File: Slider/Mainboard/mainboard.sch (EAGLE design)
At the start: 61 parts, among them IC1 7805TV, IC2 33CV, IC3 LM358, Q1 16MHz, SW1 MS MOT1, SW2 MS MOT2, T1 BC337, T2 BC337, U1 ATMEGA328P_PDIP, U2 MAX232PTH

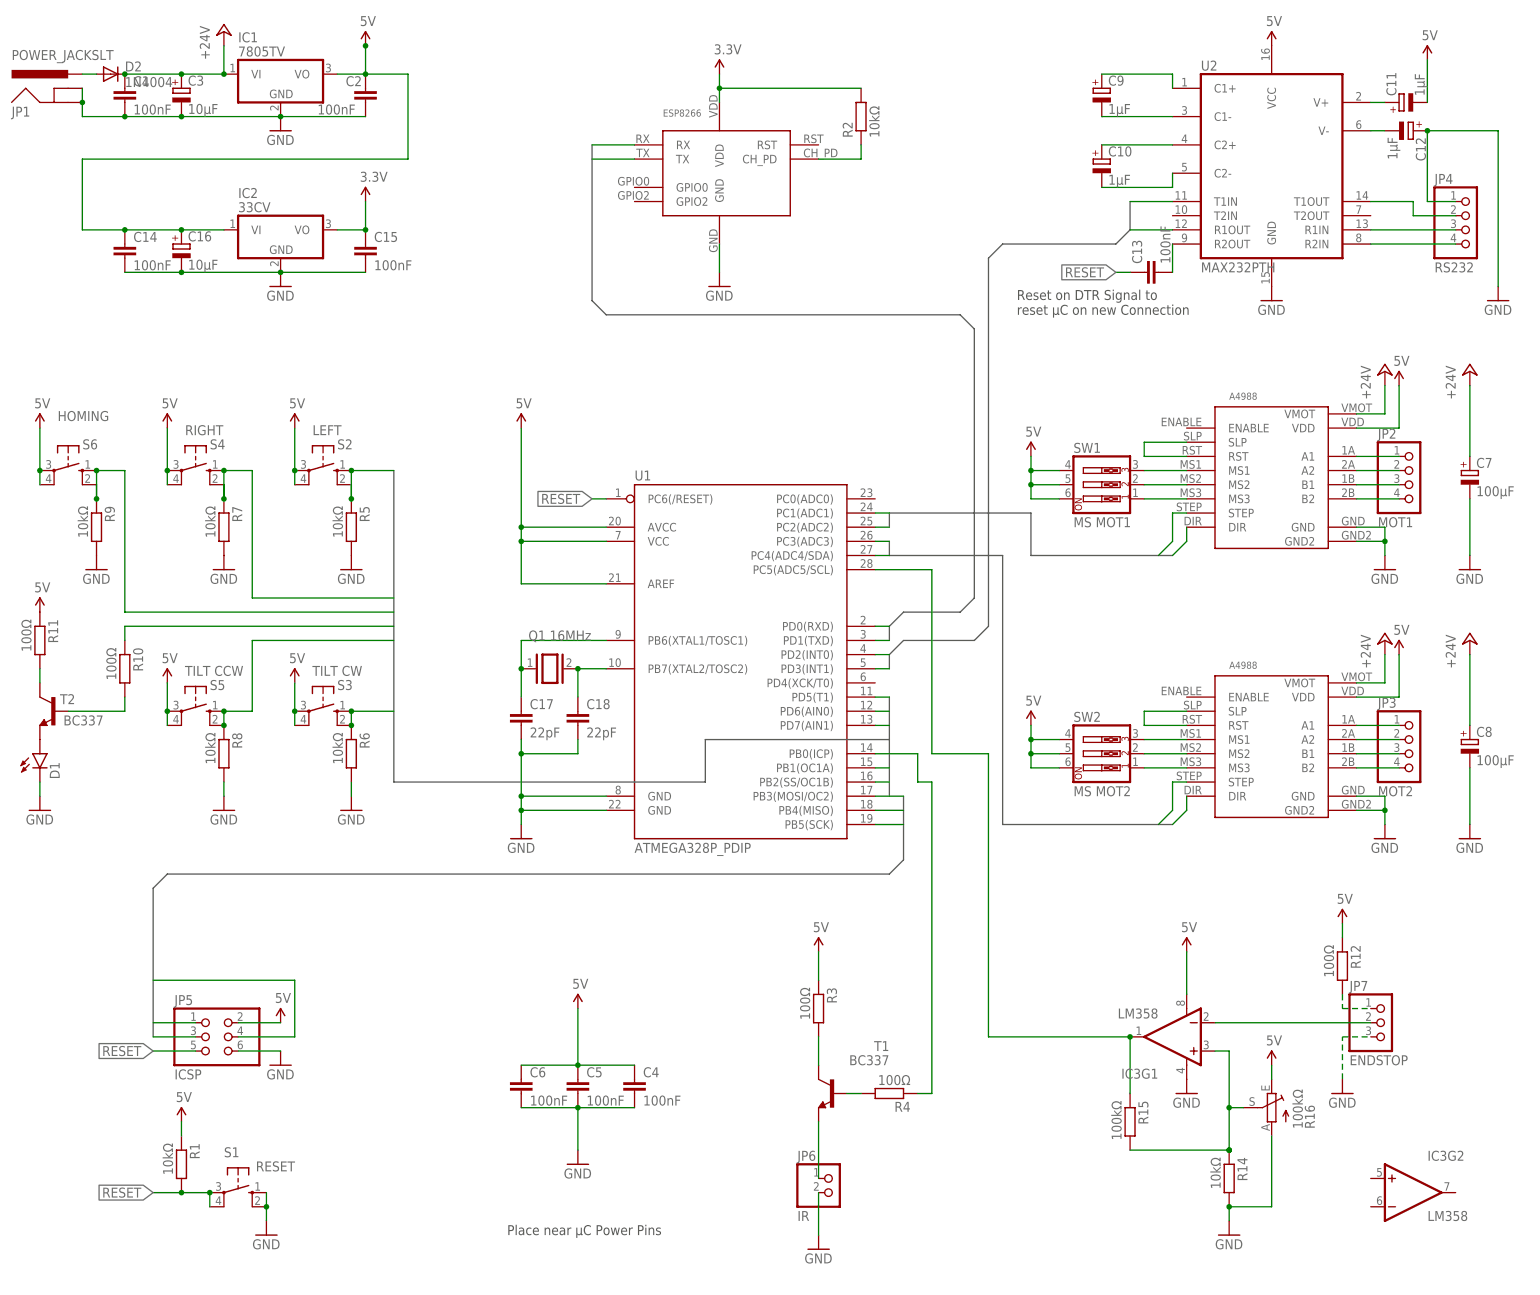
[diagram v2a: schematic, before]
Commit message: progress in board layout and schematic
- fixed the layout of the schematic after pin swapping
- board connections all done
- board layout all done
- adjusted outline to match case
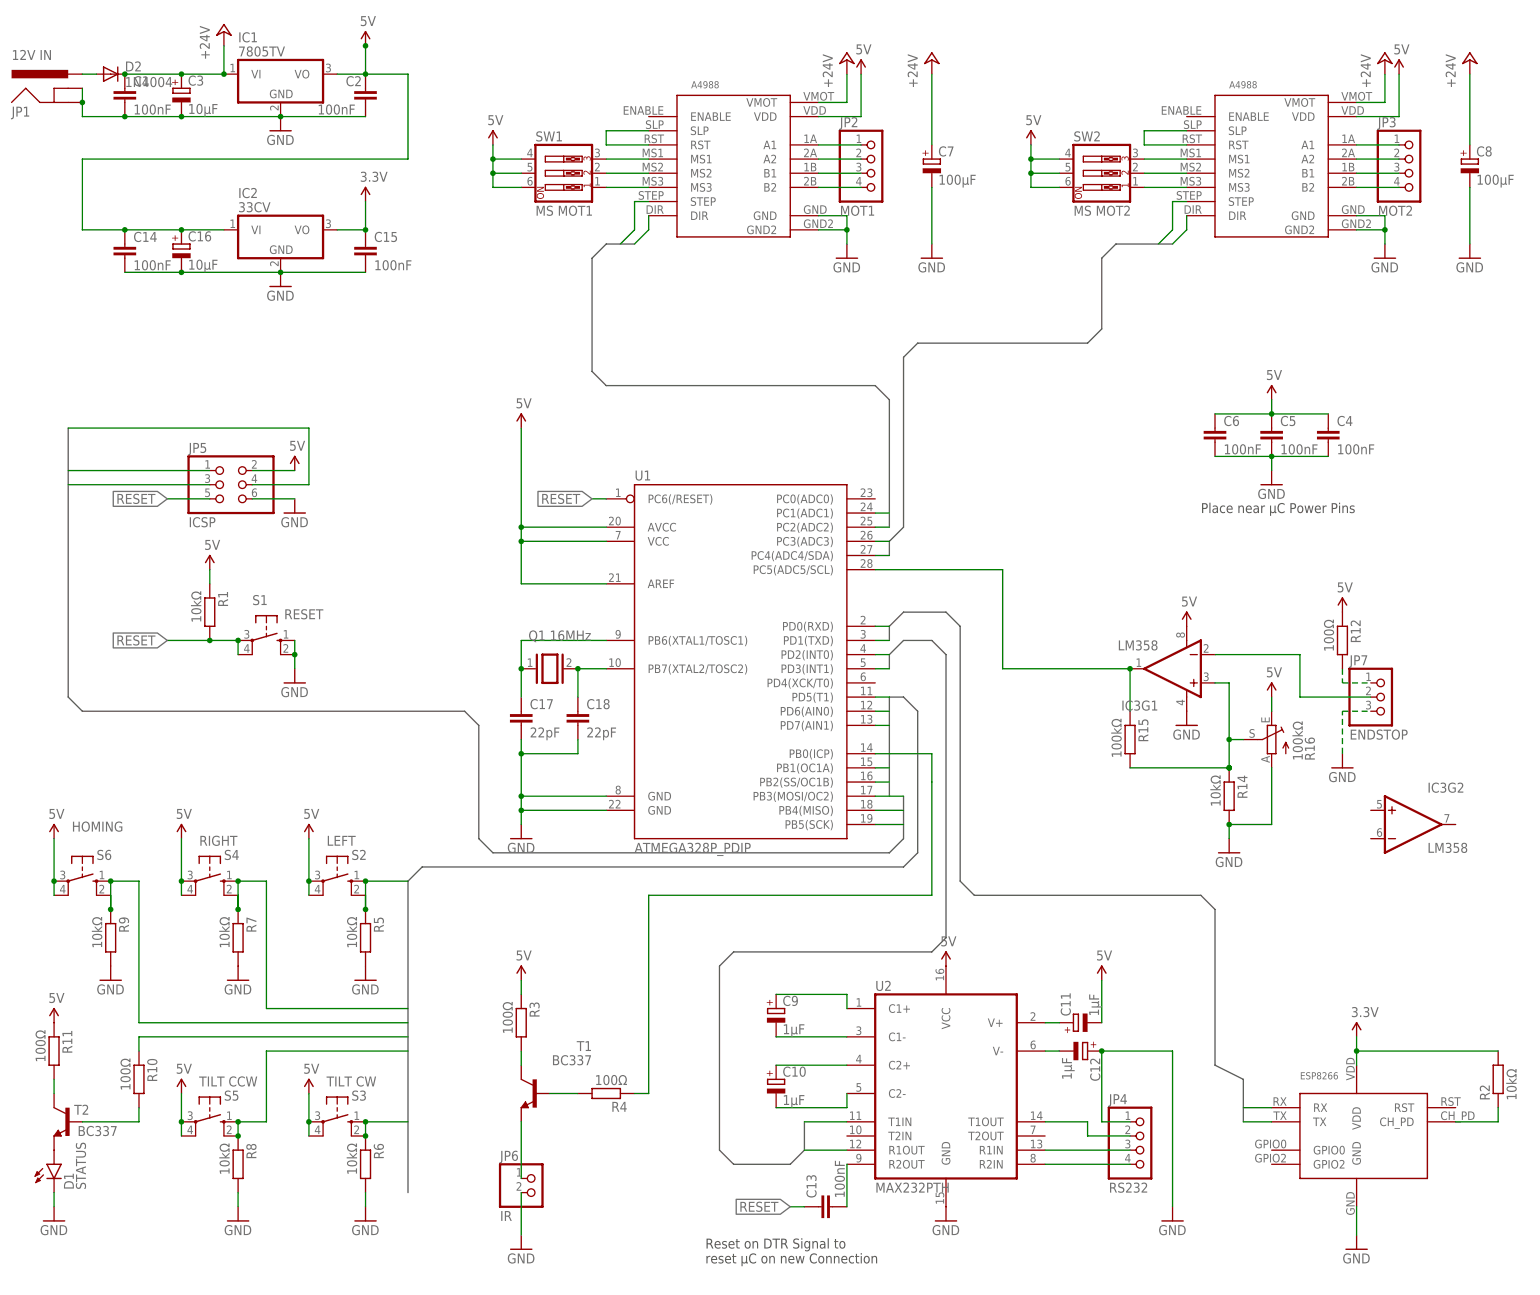
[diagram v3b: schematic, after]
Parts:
- D1: value (none) -> STATUS
- JP1: value POWER_JACKSLT -> 12V IN
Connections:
- net 5V: now also SW1.4, SW1.5, SW1.6, SW2.4, SW2.5, SW2.6
- net RXD: now also U1.PD2(INT0); no longer U1.PD3(INT1)
- net TXD: now also U1.PD3(INT1); no longer U1.PD2(INT0)
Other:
- moved on the sheet: C10, C11, C12, C13, C4, C5, C6, C7, C8, C9, D1, IC3G1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

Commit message: switched from generic pinheaders to the right connector footprint
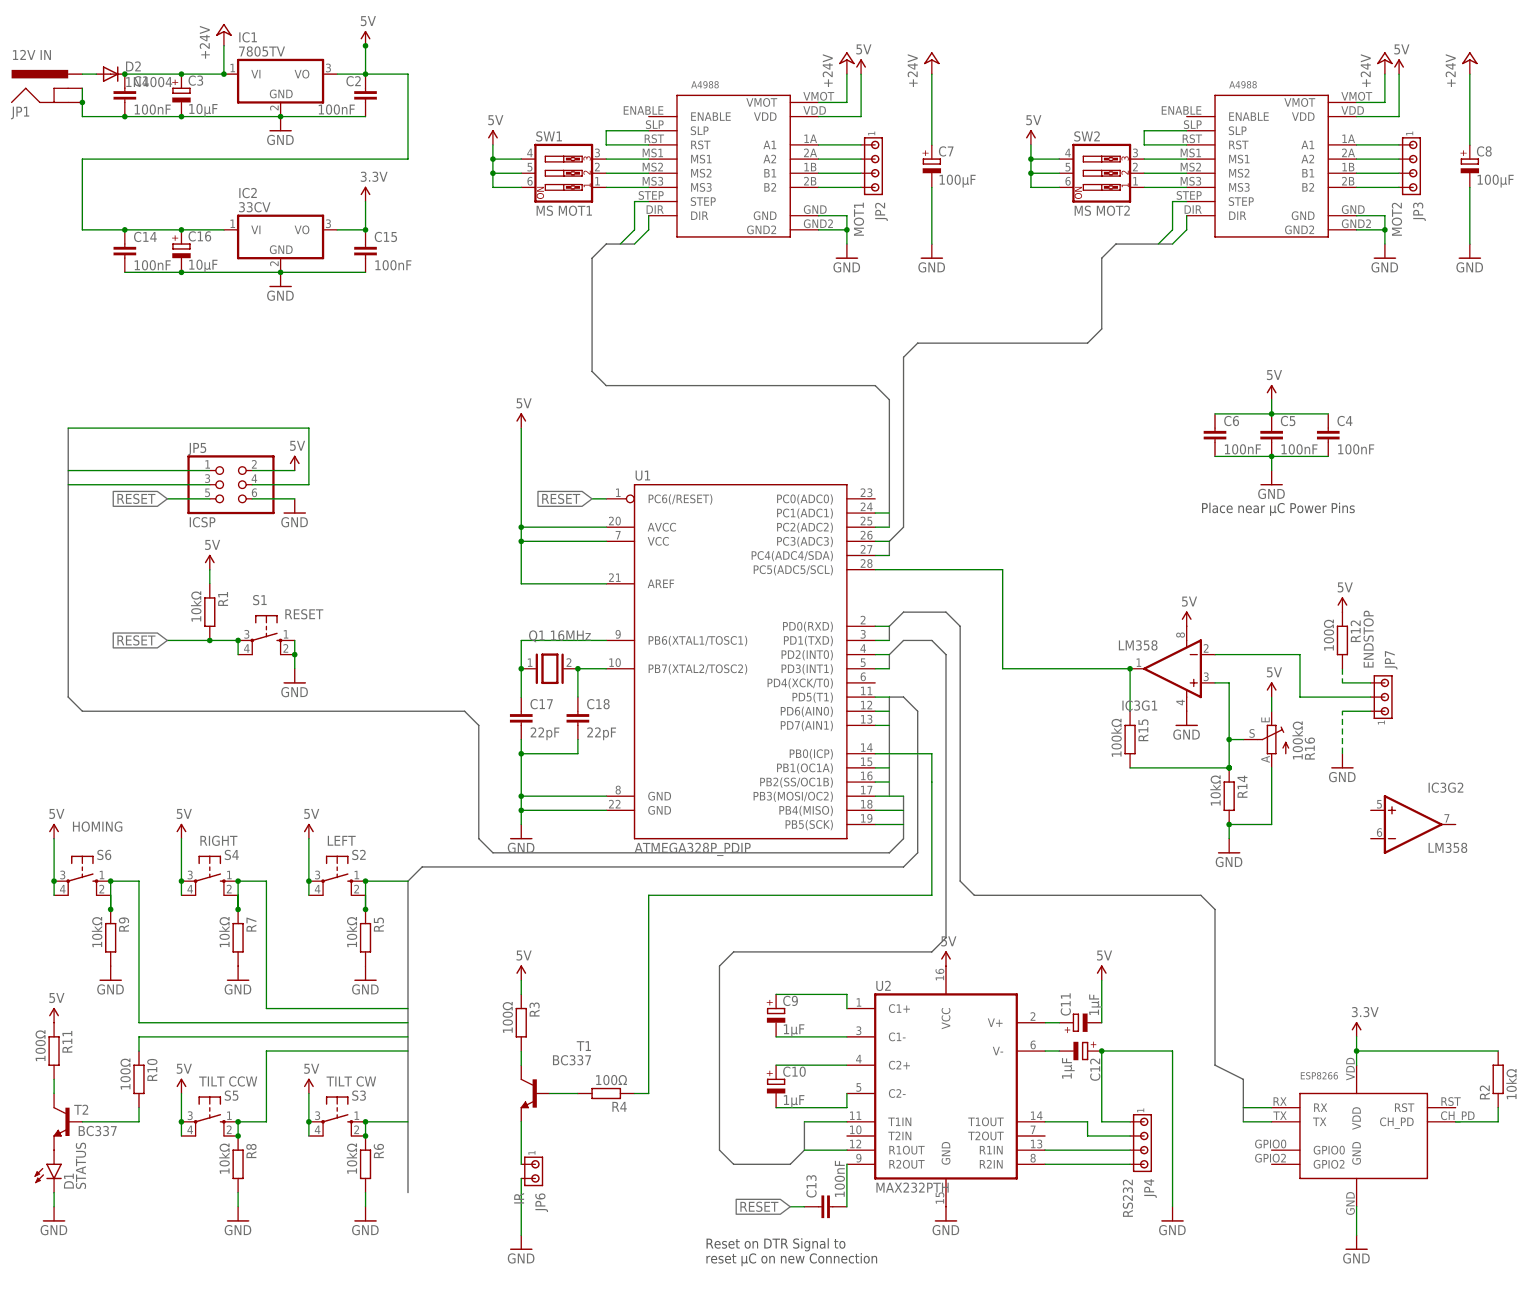
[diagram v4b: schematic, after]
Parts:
- JP2, JP3, JP4: device pinhead:PINHD-1X4 -> con-amp:MTA04-100
- JP6: device pinhead:PINHD-1X2 -> con-amp:MTA02-100
- JP7: device pinhead:PINHD-1X3 -> con-amp:MTA03-100
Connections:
- net GND: now also JP7.1; no longer JP7.3
- net N$35: now also JP7.3; no longer JP7.1
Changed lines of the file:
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@@
 <part name="SUPPLY6" library="SparkFun-Aesthetics" deviceset="5V" device=""/>
 <part name="GND5" library="supply1" deviceset="GND" device=""/>
-<part name="JP2" library="pinhead" deviceset="PINHD-1X4" device="" value="MOT1"/>
+<part name="JP2" library="con-amp" deviceset="MTA04-100" device="" value="MOT1"/>
 <part name="C7" library="rcl" deviceset="CPOL-EU" device="E2,5-6E" value="100µF"/>
 <part name="GND6" library="supply1" deviceset="GND" device=""/>
@@
 <part name="SUPPLY8" library="SparkFun-Aesthetics" deviceset="5V" device=""/>
 <part name="GND7" library="supply1" deviceset="GND" device=""/>
-<part name="JP3" library="pinhead" deviceset="PINHD-1X4" device="" value="MOT2"/>
+<part name="JP3" library="con-amp" deviceset="MTA04-100" device="" value="MOT2"/>
 <part name="C8" library="rcl" deviceset="CPOL-EU" device="E2,5-6E" value="100µF"/>
 <part name="GND8" library="supply1" deviceset="GND" device=""/>
@@
 <part name="SUPPLY11" library="SparkFun-Aesthetics" deviceset="5V" device=""/>
 <part name="GND10" library="supply1" deviceset="GND" device=""/>
-<part name="JP4" library="pinhead" deviceset="PINHD-1X4" device="" value="RS232"/>
+<part name="JP4" library="con-amp" deviceset="MTA04-100" device="" value="RS232"/>
 <part name="C13" library="rcl" deviceset="C-EU" device="050-024X044" value="100nF"/>
 <part name="JP5" library="SparkFun-Connectors" deviceset="PINHD-2X3" device="" value="ICSP"/>
@@
 <part name="SUPPLY15" library="SparkFun-Aesthetics" deviceset="5V" device=""/>
 <part name="GND14" library="supply1" deviceset="GND" device=""/>
-<part name="JP6" library="pinhead" deviceset="PINHD-1X2" device="" value="IR"/>
+<part name="JP6" library="con-amp" deviceset="MTA02-100" device="" value="IR"/>
 <part name="S2" library="switch-omron" deviceset="10-XX" device="" value="LEFT"/>
 <part name="R5" library="rcl" deviceset="R-EU_" device="0207/7" value="10kΩ"/>
@@
 <part name="R11" library="rcl" deviceset="R-EU_" device="0207/7" value="100Ω"/>
 <part name="SUPPLY21" library="SparkFun-Aesthetics" deviceset="5V" device=""/>
-<part name="JP7" library="pinhead" deviceset="PINHD-1X3" device="" value="ENDSTOP"/>
+<part name="JP7" library="con-amp" deviceset="MTA03-100" device="" value="ENDSTOP"/>
 <part name="SUPPLY22" library="SparkFun-Aesthetics" deviceset="5V" device=""/>
 <part name="R12" library="rcl" deviceset="R-EU_" device="0207/7" value="100Ω"/>
@@
 <instance part="SUPPLY6" gate="G$1" x="38.1" y="157.48"/>
 <instance part="GND5" gate="1" x="35.56" y="124.46"/>
-<instance part="JP2" gate="A" x="40.64" y="139.7"/>
+<instance part="JP2" gate="G$1" x="40.64" y="142.24" rot="R270"/>
 <instance part="C7" gate="G$1" x="50.8" y="142.24"/>
 <instance part="GND6" gate="1" x="50.8" y="124.46"/>
@@
 <instance part="SUPPLY8" gate="G$1" x="134.62" y="157.48"/>
 <instance part="GND7" gate="1" x="132.08" y="124.46"/>
-<instance part="JP3" gate="A" x="137.16" y="139.7"/>
+<instance part="JP3" gate="G$1" x="137.16" y="142.24" rot="R270"/>
 <instance part="C8" gate="G$1" x="147.32" y="142.24"/>
 <instance part="GND8" gate="1" x="147.32" y="124.46"/>
@@
 <instance part="SUPPLY11" gate="G$1" x="81.28" y="-5.08"/>
 <instance part="GND10" gate="1" x="93.98" y="-48.26"/>
-<instance part="JP4" gate="A" x="88.9" y="-35.56"/>
+<instance part="JP4" gate="G$1" x="88.9" y="-33.02" rot="R270"/>
 <instance part="C13" gate="G$1" x="30.48" y="-45.72" rot="R90"/>
 <instance part="JP5" gate="A" x="-76.2" y="83.82"/>
@@
 <instance part="SUPPLY15" gate="G$1" x="-22.86" y="-5.08"/>
 <instance part="GND14" gate="1" x="-22.86" y="-53.34"/>
-<instance part="JP6" gate="G$1" x="-20.32" y="-43.18"/>
+<instance part="JP6" gate="G$1" x="-20.32" y="-38.1" rot="R270"/>
 <instance part="S2" gate="1" x="-55.88" y="12.7" smashed="yes" rot="R270">
 <attribute name="NAME" x="-53.34" y="16.51" size="1.778" layer="95"/>
@@
 <instance part="R11" gate="G$1" x="-106.68" y="-17.78" rot="R270"/>
 <instance part="SUPPLY21" gate="G$1" x="-106.68" y="-12.7"/>
-<instance part="JP7" gate="A" x="132.08" y="45.72"/>
+<instance part="JP7" gate="G$1" x="132.08" y="45.72" rot="MR90"/>
 <instance part="SUPPLY22" gate="G$1" x="124.46" y="60.96"/>
 <instance part="R12" gate="G$1" x="124.46" y="55.88" rot="R270"/>
@@
 <pinref part="JP6" gate="G$1" pin="2"/>
 <pinref part="GND14" gate="1" pin="GND"/>
-<wire x1="-22.86" y1="-50.8" x2="-22.86" y2="-43.18" width="0.1524" layer="91"/>
+<wire x1="-22.86" y1="-50.8" x2="-22.86" y2="-40.64" width="0.1524" layer="91"/>
 </segment>
 <segment>
@@
 <pinref part="GND21" gate="1" pin="GND"/>
 <wire x1="124.46" y1="35.56" x2="124.46" y2="43.18" width="0.1524" layer="91" style="longdash"/>
-<pinref part="JP7" gate="A" pin="3"/>
-<wire x1="124.46" y1="43.18" x2="129.54" y2="43.18" width="0.1524" layer="91" style="longdash"/>
+<pinref part="JP7" gate="G$1" pin="1"/>
+<wire x1="129.54" y1="43.18" x2="124.46" y2="43.18" width="0.1524" layer="91"/>
 </segment>
 <segment>
@@
 <wire x1="93.98" y1="-45.72" x2="93.98" y2="-17.78" width="0.1524" layer="91"/>
 <pinref part="C12" gate="G$1" pin="+"/>
-<pinref part="JP4" gate="A" pin="1"/>
+<pinref part="JP4" gate="G$1" pin="1"/>
 <wire x1="86.36" y1="-30.48" x2="81.28" y2="-30.48" width="0.1524" layer="91"/>
 <wire x1="81.28" y1="-30.48" x2="81.28" y2="-17.78" width="0.1524" layer="91"/>
@@
 <segment>
 <pinref part="U$1" gate="G$1" pin="A1"/>
-<pinref part="JP2" gate="A" pin="1"/>
+<pinref part="JP2" gate="G$1" pin="1"/>
 <wire x1="38.1" y1="144.78" x2="30.48" y2="144.78" width="0.1524" layer="91"/>
 </segment>
@@
 <segment>
 <pinref part="U$1" gate="G$1" pin="A2"/>
-<pinref part="JP2" gate="A" pin="2"/>
+<pinref part="JP2" gate="G$1" pin="2"/>
 <wire x1="38.1" y1="142.24" x2="30.48" y2="142.24" width="0.1524" layer="91"/>
 </segment>
@@
 <segment>
 <pinref part="U$1" gate="G$1" pin="B1"/>
-<pinref part="JP2" gate="A" pin="3"/>
+<pinref part="JP2" gate="G$1" pin="3"/>
 <wire x1="38.1" y1="139.7" x2="30.48" y2="139.7" width="0.1524" layer="91"/>
 </segment>
@@
 <segment>
 <pinref part="U$1" gate="G$1" pin="B2"/>
-<pinref part="JP2" gate="A" pin="4"/>
+<pinref part="JP2" gate="G$1" pin="4"/>
 <wire x1="38.1" y1="137.16" x2="30.48" y2="137.16" width="0.1524" layer="91"/>
 </segment>
@@
 <segment>
 <pinref part="U$2" gate="G$1" pin="A1"/>
-<pinref part="JP3" gate="A" pin="1"/>
+<pinref part="JP3" gate="G$1" pin="1"/>
 <wire x1="134.62" y1="144.78" x2="127" y2="144.78" width="0.1524" layer="91"/>
 </segment>
@@
 <segment>
 <pinref part="U$2" gate="G$1" pin="A2"/>
-<pinref part="JP3" gate="A" pin="2"/>
+<pinref part="JP3" gate="G$1" pin="2"/>
 <wire x1="134.62" y1="142.24" x2="127" y2="142.24" width="0.1524" layer="91"/>
 </segment>
@@
 <segment>
 <pinref part="U$2" gate="G$1" pin="B1"/>
-<pinref part="JP3" gate="A" pin="3"/>
+<pinref part="JP3" gate="G$1" pin="3"/>
 <wire x1="134.62" y1="139.7" x2="127" y2="139.7" width="0.1524" layer="91"/>
 </segment>
@@
 <segment>
 <pinref part="U$2" gate="G$1" pin="B2"/>
-<pinref part="JP3" gate="A" pin="4"/>
+<pinref part="JP3" gate="G$1" pin="4"/>
 <wire x1="134.62" y1="137.16" x2="127" y2="137.16" width="0.1524" layer="91"/>
 </segment>
@@
 <net name="N$18" class="0">
 <segment>
-<pinref part="JP4" gate="A" pin="2"/>
+<pinref part="JP4" gate="G$1" pin="2"/>
 <wire x1="86.36" y1="-33.02" x2="78.74" y2="-33.02" width="0.1524" layer="91"/>
 <wire x1="78.74" y1="-33.02" x2="78.74" y2="-30.48" width="0.1524" layer="91"/>
@@
 <net name="N$19" class="0">
 <segment>
-<pinref part="JP4" gate="A" pin="3"/>
+<pinref part="JP4" gate="G$1" pin="3"/>
 <pinref part="U2" gate="G$1" pin="R1IN"/>
 <wire x1="86.36" y1="-35.56" x2="71.12" y2="-35.56" width="0.1524" layer="91"/>
@@
 <net name="N$26" class="0">
 <segment>
-<pinref part="JP4" gate="A" pin="4"/>
+<pinref part="JP4" gate="G$1" pin="4"/>
 <pinref part="U2" gate="G$1" pin="R2IN"/>
 <wire x1="86.36" y1="-38.1" x2="71.12" y2="-38.1" width="0.1524" layer="91"/>
@@
 <pinref part="T1" gate="G$1" pin="E"/>
 <pinref part="JP6" gate="G$1" pin="1"/>
-<wire x1="-22.86" y1="-30.48" x2="-22.86" y2="-40.64" width="0.1524" layer="91"/>
+<wire x1="-22.86" y1="-30.48" x2="-22.86" y2="-38.1" width="0.1524" layer="91"/>
 </segment>
 </net>
@@
 <segment>
 <pinref part="R12" gate="G$1" pin="2"/>
-<pinref part="JP7" gate="A" pin="1"/>
 <wire x1="124.46" y1="50.8" x2="124.46" y2="48.26" width="0.1524" layer="91" style="longdash"/>
-<wire x1="124.46" y1="48.26" x2="129.54" y2="48.26" width="0.1524" layer="91" style="longdash"/>
+<pinref part="JP7" gate="G$1" pin="3"/>
+<wire x1="129.54" y1="48.26" x2="124.46" y2="48.26" width="0.1524" layer="91"/>
 </segment>
 </net>
@@
 <wire x1="116.84" y1="53.34" x2="116.84" y2="45.72" width="0.1524" layer="91"/>
 <wire x1="116.84" y1="45.72" x2="129.54" y2="45.72" width="0.1524" layer="91"/>
-<pinref part="JP7" gate="A" pin="2"/>
-</segment>
-</net>
+<pinref part="JP7" gate="G$1" pin="2"/>
+</segment>
+</net>
